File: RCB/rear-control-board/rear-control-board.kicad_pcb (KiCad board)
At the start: 2 copper layers, 99.1 x 99.1 mm, 58 parts, among them J1 Conn_01x23, J2 Conn_01x14, J3 Conn_01x08, J4 Conn_01x02, J5 Conn_01x02, J6 Conn_01x05, K1 T9VV1K15-12S, K2 G5V-2, K3 G5V-2, Q1 BSS84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

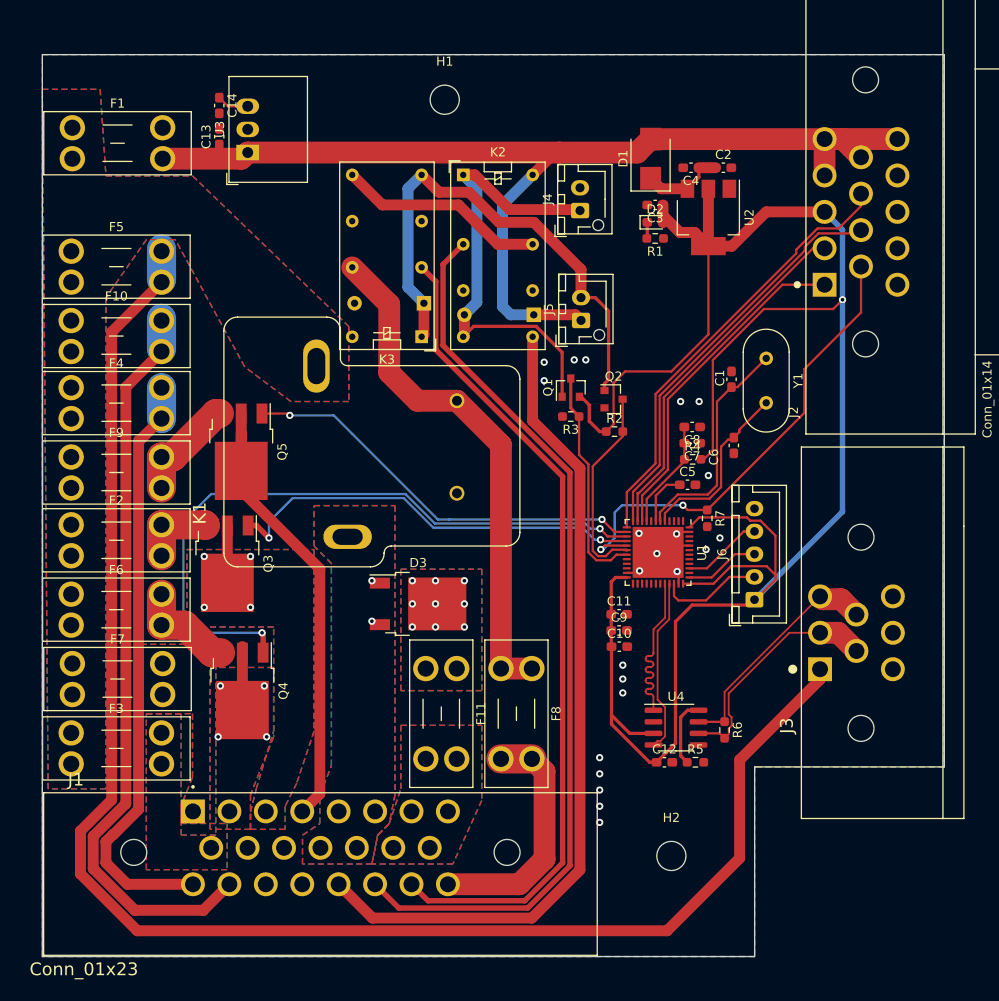
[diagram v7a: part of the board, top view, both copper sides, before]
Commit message: updating filtering cap layout
Kay suggested layout changes. Moved caps around
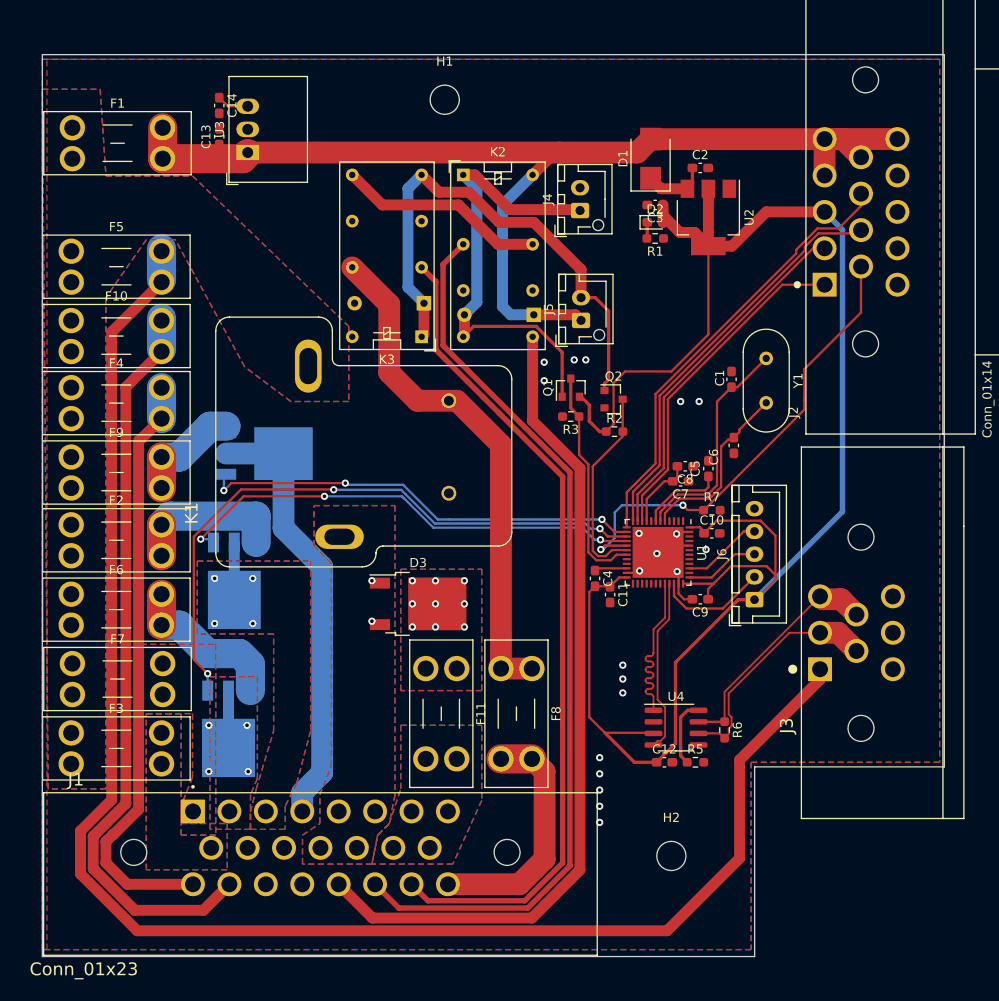
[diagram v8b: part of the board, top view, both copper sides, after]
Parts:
- removed R4: R, Resistor_SMD:R_0603_1608Metric_Pad0.98x0.95mm_HandSolder
- C2: value C -> .1u
- C3: value C -> 10u
- C4: value CP1 -> 4.7u
- Q3, Q4, Q5: moved to B.Cu
- R1: value R -> 220
- moved C4 46.3 mm to (121.7, 98.2), turned to -90 degrees
- moved C10 16.1 mm to (134.5, 93.2)
- moved C9 9.55 mm to (133.2, 100.5), turned to 180 degrees
- moved Q4 4.43 mm to (81.4, 114.7)
- moved C8 4.38 mm to (131.6, 85.9)
- moved C7 4.38 mm to (131.1, 87.5)
- moved C5 2.90 mm to (134.1, 86.1), turned to 90 degrees
- moved Q5 2.55 mm to (85.3, 84.5), turned to 0 degrees
- moved C2 2.54 mm to (133.2, 53.1)
- moved C11 2.37 mm to (123.3, 99.9), turned to -90 degrees
- moved Q3 2.02 mm to (82.0, 98.4)
- moved R7 1.02 mm to (134.5, 90.7), turned to 0 degrees
- moved K1 0.89 mm to (93.6, 84.2)
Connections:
- C4 pad 1: Net-(C2-Pad1) -> Net-(U1-Pad22)
- C4 pad 2: GND -> +3V3
- U1 pad 22: unconnected-(U1-Pad22) -> Net-(U1-Pad22)
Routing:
- net +3V3: track 224.3 -> 199.1 mm, vias 1 -> 0
- net /FAN_12V: track 8.26 -> 17.1 mm
- net /PUMP_12V: track 11.1 -> 17.8 mm
- net /Controller/PUMP_CTRL: track 74.2 -> 69.4 mm, vias 2 -> 3
- net /Controller/FAN_CTRL: track 47.6 -> 52.3 mm, vias 2 -> 3
- net VDD: track 119.5 -> 123.8 mm
- net Net-(C7-Pad2): track 12.1 -> 7.96 mm
- net /BRAKE_CTRL_12V: track 52.2 -> 48.3 mm
- net Net-(U1-Pad22): track 0.00 -> 3.58 mm
- net Net-(C5-Pad1): track 5.91 -> 9.17 mm
- net /Controller/BRAKE_CTRL: track 45.4 -> 48.7 mm, vias 2 -> 3
- net Net-(C2-Pad1): track 9.24 -> 6.26 mm
- net GND: track 16.9 -> 19.7 mm, vias 22 -> 20
- net /FAN_CTRL_12V: track 7.97 -> 6.30 mm
- net A13_SWDIO: track 11.5 -> 12.2 mm
